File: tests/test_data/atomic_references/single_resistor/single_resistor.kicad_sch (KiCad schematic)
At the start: 1 part

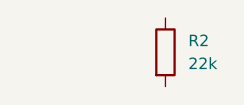
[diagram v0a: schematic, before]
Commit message: ✅ Add comprehensive unit tests and reference projects for atomic operations
## Test Coverage Expansion 🧪
- 23 total tests across 3 test files (all passing)
- Comprehensive validation of atomic operations lifecycle
- Reference schematic comparison and validation
- Production integration testing

## New Test Files 📋
- test_atomic_operations_comprehensive.py: 10 comprehensive tests
  * Reference schematic validation
  * Complete atomic operation cycles (blank→single→two→single→blank)
  * Mixed component type testing
  * Error handling and atomic safety
- test_atomic_integration.py: 9 production integration tests
  * AtomicKiCadIntegration class testing
  * JSON pipeline integration
  * Hierarchical sheet management
  * Error handling and backup/restore

## Reference Projects 📚
- Copied reference KiCad projects to tests/test_data/atomic_references/
  * blank_schematic/: Minimal empty schematic
  * single_resistor/: Single 10k resistor component
  * two_resistors/: Two resistor components
- Smart schematic analysis function with lib_symbols filtering
- Robust component reference detection and validation

## Test Validation ✅
- All atomic operations work correctly with reference validation
- Proper component addition/removal lifecycle verified
- Integration with circuit-synth pipeline confirmed
- Error handling and atomic safety validated
- Reference schematic compatibility confirmed

## Key Features Tested 🔍
- Exact S-expression manipulation vs reference schematics
- Hierarchical sheet reference management
- Component lifecycle (add→modify→remove)
- Production pipeline integration
- Error recovery and file integrity protection

The atomic operations system now has comprehensive test coverage
with reference validation ensuring reliability and correctness!

🤖 Generated with [Claude Code](https://claude.ai/code)

Co-Authored-By: Claude <noreply@anthropic.com>
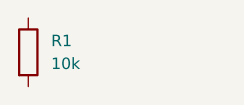
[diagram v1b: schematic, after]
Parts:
- removed R2: 22k, Resistor_SMD:R_0603_1608Metric, symbol Device:R
- added R1: 10k, Resistor_SMD:R_0603_1608Metric, symbol Device:R
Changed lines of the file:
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@@
 	(symbol
 		(lib_id "Device:R")
-		(at 137.16 68.58 0)
+		(at 121.92 68.58 0)
 		(unit 1)
 		(exclude_from_sim no)
@@
 		(dnp no)
 		(fields_autoplaced yes)
-		(property "Reference" "R2"
-			(at 139.7 67.3099 0)
+		(property "Reference" "R1"
+			(at 124.46 67.3099 0)
 			(effects
 				(font
@@
 			)
 		)
-		(property "Value" "22k"
-			(at 139.7 69.8599 0)
+		(property "Value" "10k"
+			(at 124.46 69.8499 0)
 			(effects
 				(font
@@
 		)
 		(property "Footprint" "Resistor_SMD:R_0603_1608Metric"
-			(at 135.382 68.58 90)
+			(at 120.142 68.58 90)
 			(effects
 				(font
@@
 		)
 		(property "Datasheet" "~"
-			(at 137.16 68.58 0)
+			(at 121.92 68.58 0)
 			(effects
 				(font
@@
 		)
 		(property "Description" "Resistor"
-			(at 137.16 68.58 0)
+			(at 121.92 68.58 0)
 			(effects
 				(font
@@
 		(instances
 			(project ""
-				(path "/c607e5f1-42e2-4249-b659-6d0555bce224"
-					(reference "R2")
+				(path "/276f8821-4c7d-4bd9-a39c-2b6212c3a3a2"
+					(reference "R1")
 					(unit 1)
 				)
